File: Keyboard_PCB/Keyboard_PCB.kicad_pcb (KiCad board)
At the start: 4 copper layers, 305 x 132 mm, 1 part

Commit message: Keypad schematic progress
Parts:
- removed REF**: EC11E-Switch_No_MP, Custom:EC11E-Switch_No_MP
- added C14: 10u, Capacitor_SMD:C_0603_1608Metric, F.Cu at (181.6, 152.0)
- added C15: 56p, Capacitor_SMD:C_0603_1608Metric, F.Cu at (181.6, 154.5)
- added C16: 22u, Capacitor_SMD:C_0603_1608Metric, F.Cu at (181.6, 157.1)
- added C17: 22u, Capacitor_SMD:C_0603_1608Metric, F.Cu at (181.6, 159.6)
- added C18: 100n, Capacitor_SMD:C_0603_1608Metric, F.Cu at (242.3, 128.0)
- added C19: 12p, Capacitor_SMD:C_0603_1608Metric, F.Cu at (242.3, 130.5)
- added C20: 12p, Capacitor_SMD:C_0603_1608Metric, F.Cu at (242.3, 133.0)
- added C21: 12p, Capacitor_SMD:C_0603_1608Metric, F.Cu at (242.3, 135.5)
- added C22: 12p, Capacitor_SMD:C_0603_1608Metric, F.Cu at (242.3, 138.0)
- added D1: D_Small, Diode_SMD:D_SOD-323, F.Cu at (112.6, 101.9)
- added D10: D_Small, Diode_SMD:D_SOD-323, F.Cu at (121.2, 104.8)
- added D11: D_Small, Diode_SMD:D_SOD-323, F.Cu at (121.2, 107.8)
- added D12: D_Small, Diode_SMD:D_SOD-323, F.Cu at (121.2, 110.7)
- added D2: D_Small, Diode_SMD:D_SOD-323, F.Cu at (112.6, 104.8)
- added D3: D_Small, Diode_SMD:D_SOD-323, F.Cu at (112.6, 107.8)
- added D4: D_Small, Diode_SMD:D_SOD-323, F.Cu at (112.6, 110.7)
- added D5: D_Small, Diode_SMD:D_SOD-323, F.Cu at (116.9, 101.9)
- added D6: D_Small, Diode_SMD:D_SOD-323, F.Cu at (116.9, 104.8)
- added D7: D_Small, Diode_SMD:D_SOD-323, F.Cu at (116.9, 107.8)
- added D8: D_Small, Diode_SMD:D_SOD-323, F.Cu at (116.9, 110.7)
- added D9: D_Small, Diode_SMD:D_SOD-323, F.Cu at (121.2, 101.9)
- added J5: Conn_ARM_SWD_TagConnect_TC2030, Connector:Tag-Connect_TC2030-IDC-FP_2x03_P1.27mm_Vertical, F.Cu at (249.1, 131.5)
- added J6: CH_USB_C, Connector_USB:USB_C_Receptacle_HCTL_HC-TYPE-C-16P-01A, F.Cu at (211.9, 89.0)
- added L3: 1u, Inductor_SMD:L_APV_ANR4018, F.Cu at (186.5, 159.8)
- added R10: 10k, Resistor_SMD:R_0603_1608Metric, F.Cu at (242.3, 143.0)
- added R11: 320k, Resistor_SMD:R_0603_1608Metric, F.Cu at (181.6, 164.6)
- added R12: 5k1, Resistor_SMD:R_0603_1608Metric, F.Cu at (213.3, 94.9)
- added R8: 10k, Resistor_SMD:R_0603_1608Metric, F.Cu at (242.3, 140.5)
- added R9: 1M, Resistor_SMD:R_0603_1608Metric, F.Cu at (181.6, 162.1)
- added SW1: 0, Button_Switch_Keyboard:SW_Cherry_MX_1.00u_PCB, F.Cu at (134.5, 87.2)
- added SW10: 9, Button_Switch_Keyboard:SW_Cherry_MX_1.00u_PCB, F.Cu at (179.8, 87.2)
- added SW11: 10, Button_Switch_Keyboard:SW_Cherry_MX_1.00u_PCB, F.Cu at (179.8, 102.3)
- added SW12: 11, Button_Switch_Keyboard:SW_Cherry_MX_1.00u_PCB, F.Cu at (179.8, 117.4)
- added SW13: BOOT, Button_Switch_SMD:SW_SPST_PTS810, F.Cu at (247.7, 138.6)
- added SW14: NRST, Button_Switch_SMD:SW_SPST_PTS810, F.Cu at (247.7, 143.4)
- added SW2: 1, Button_Switch_Keyboard:SW_Cherry_MX_1.00u_PCB, F.Cu at (134.5, 102.3)
- added SW3: 2, Button_Switch_Keyboard:SW_Cherry_MX_1.00u_PCB, F.Cu at (134.5, 117.4)
- added SW4: 3, Button_Switch_Keyboard:SW_Cherry_MX_1.00u_PCB, F.Cu at (149.6, 87.2)
- added SW5: 4, Button_Switch_Keyboard:SW_Cherry_MX_1.00u_PCB, F.Cu at (149.6, 102.3)
- added SW6: 5, Button_Switch_Keyboard:SW_Cherry_MX_1.00u_PCB, F.Cu at (149.6, 117.4)
- added SW7: 6, Button_Switch_Keyboard:SW_Cherry_MX_1.00u_PCB, F.Cu at (164.7, 87.2)
- added SW8: 7, Button_Switch_Keyboard:SW_Cherry_MX_1.00u_PCB, F.Cu at (164.7, 102.3)
- added SW9: 8, Button_Switch_Keyboard:SW_Cherry_MX_1.00u_PCB, F.Cu at (164.7, 117.4)
- added TP1: 3V3, TestPoint:TestPoint_Pad_D1.5mm, F.Cu at (191.1, 158.8)
- added U1: STM32U385VGI6, Marijn:UFBGA-100_7x7mm, F.Cu at (149.0, 163.3)
- added U2: EMMC32G-TS0A-01002, Marijn:FBGA153_13X11.5X0.8, F.Cu at (134.8, 161.9)
- added U3: ISL91127IRAZ, Package_DFN_QFN:QFN-20-1EP_4x4mm_P0.5mm_EP2.7x2.7mm_ThermalVias, F.Cu at (186.8, 153.9)
- added U6: USBLC6-2SC6, Package_TO_SOT_SMD:SOT-23-6, F.Cu at (208.7, 96.1)
- added Y3: 25MHz, Crystal:Crystal_SMD_3225-4Pin_3.2x2.5mm, F.Cu at (253.7, 138.5)
- added Y4: 32.786KHz, Crystal:Crystal_SMD_3215-2Pin_3.2x1.5mm, F.Cu at (253.6, 142.5)
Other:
- board outline removed
- copper layers 4 -> 6

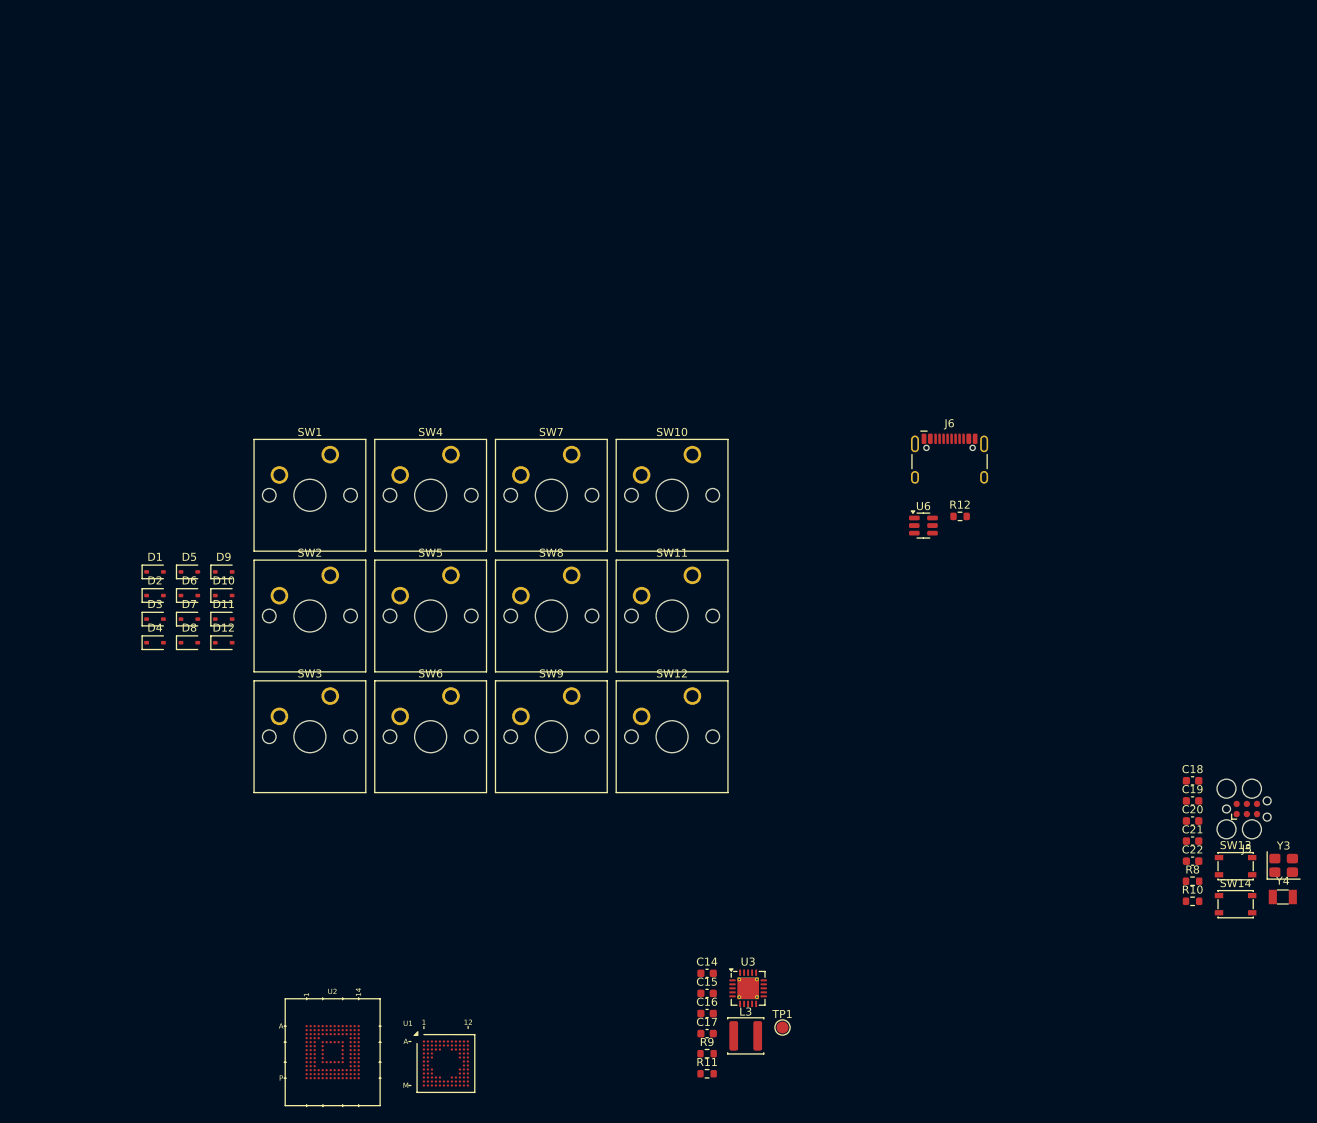
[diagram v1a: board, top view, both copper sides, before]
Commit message: STM32U385 pin assignment progress
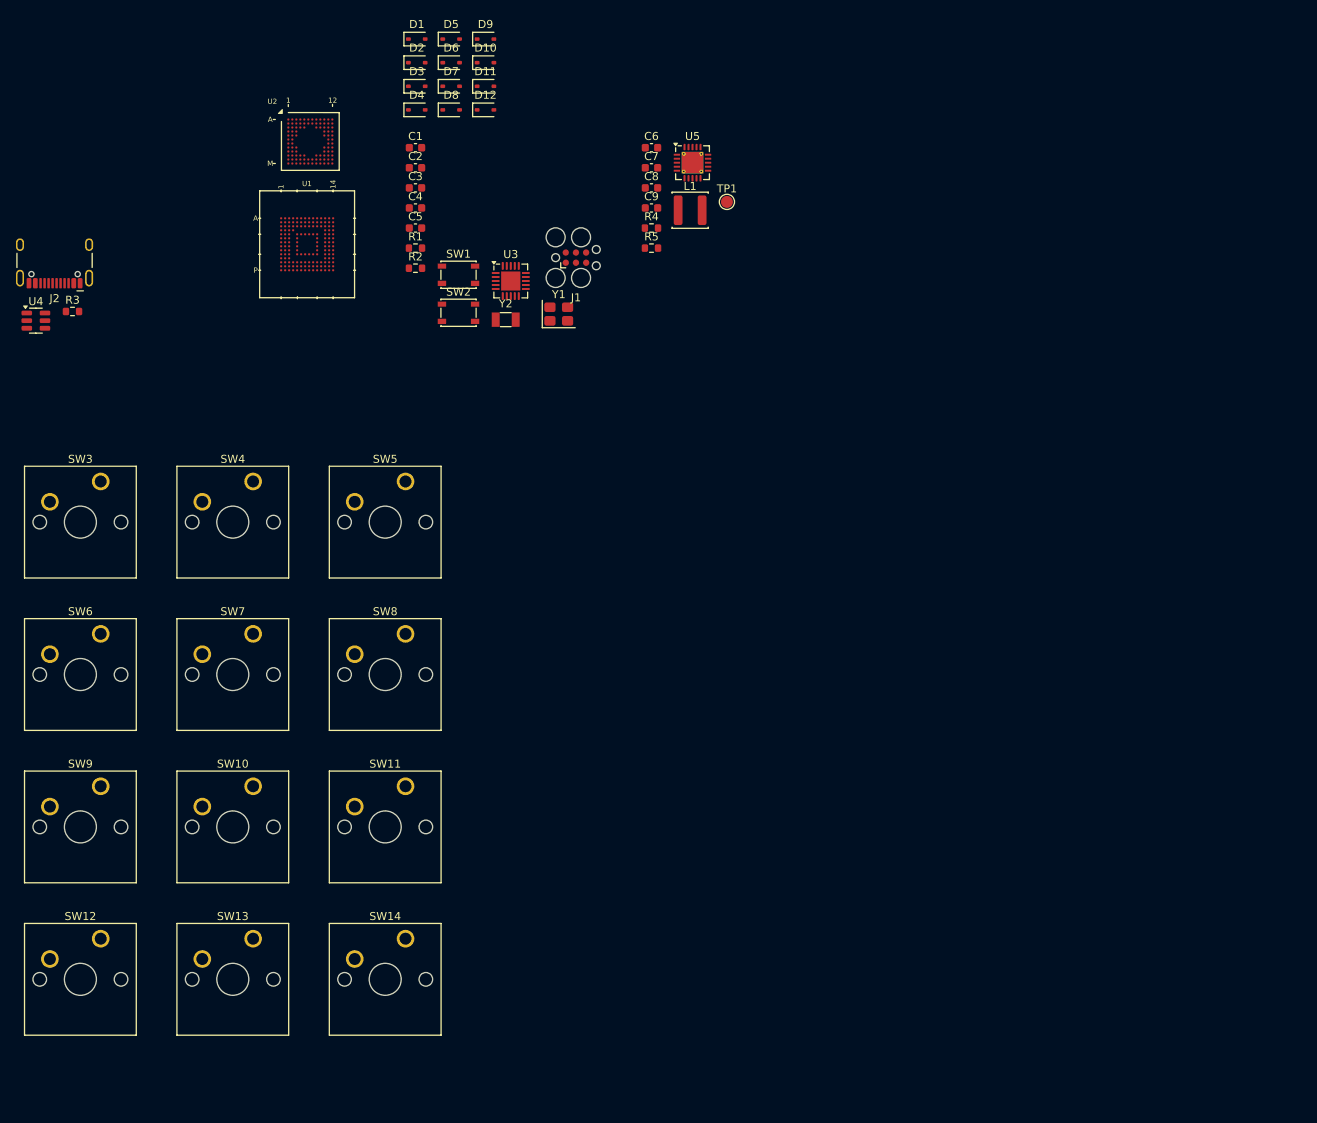
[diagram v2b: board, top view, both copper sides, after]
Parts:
- removed C14: 10u, Capacitor_SMD:C_0603_1608Metric
- removed C15: 56p, Capacitor_SMD:C_0603_1608Metric
- removed C16, C17: 22u, Capacitor_SMD:C_0603_1608Metric
- removed C18: 100n, Capacitor_SMD:C_0603_1608Metric
- removed C19, C20, C21, C22: 12p, Capacitor_SMD:C_0603_1608Metric
- removed J5: Conn_ARM_SWD_TagConnect_TC2030, Connector:Tag-Connect_TC2030-IDC-FP_2x03_P1.27mm_Vertical
- removed J6: CH_USB_C, Connector_USB:USB_C_Receptacle_HCTL_HC-TYPE-C-16P-01A
- removed L3: 1u, Inductor_SMD:L_APV_ANR4018
- removed R10, R8: 10k, Resistor_SMD:R_0603_1608Metric
- removed R11: 320k, Resistor_SMD:R_0603_1608Metric
- removed R12: 5k1, Resistor_SMD:R_0603_1608Metric
- removed R9: 1M, Resistor_SMD:R_0603_1608Metric
- removed U6: USBLC6-2SC6, Package_TO_SOT_SMD:SOT-23-6
- removed Y3: 25MHz, Crystal:Crystal_SMD_3225-4Pin_3.2x2.5mm
- removed Y4: 32.786KHz, Crystal:Crystal_SMD_3215-2Pin_3.2x1.5mm
- added C1: 100n, Capacitor_SMD:C_0603_1608Metric, F.Cu at (145.2, 48.8)
- added C2: 12p, Capacitor_SMD:C_0603_1608Metric, F.Cu at (145.2, 51.3)
- added C3: 12p, Capacitor_SMD:C_0603_1608Metric, F.Cu at (145.2, 53.8)
- added C4: 12p, Capacitor_SMD:C_0603_1608Metric, F.Cu at (145.2, 56.4)
- added C5: 12p, Capacitor_SMD:C_0603_1608Metric, F.Cu at (145.2, 58.9)
- added C6: 10u, Capacitor_SMD:C_0603_1608Metric, F.Cu at (174.7, 48.8)
- added C7: 56p, Capacitor_SMD:C_0603_1608Metric, F.Cu at (174.7, 51.3)
- added C8: 22u, Capacitor_SMD:C_0603_1608Metric, F.Cu at (174.7, 53.8)
- added C9: 22u, Capacitor_SMD:C_0603_1608Metric, F.Cu at (174.7, 56.4)
- added J1: Conn_ARM_SWD_TagConnect_TC2030, Connector:Tag-Connect_TC2030-IDC-FP_2x03_P1.27mm_Vertical, F.Cu at (165.2, 62.6)
- added J2: CH_USB_C, Connector_USB:USB_C_Receptacle_HCTL_HC-TYPE-C-16P-01A, F.Cu at (100.1, 62.0)
- added L1: 1u, Inductor_SMD:L_APV_ANR4018, F.Cu at (179.5, 56.6)
- added R1: 10k, Resistor_SMD:R_0603_1608Metric, F.Cu at (145.2, 61.4)
- added R2: 10k, Resistor_SMD:R_0603_1608Metric, F.Cu at (145.2, 63.9)
- added R3: 5k1, Resistor_SMD:R_0603_1608Metric, F.Cu at (102.3, 69.3)
- added R4: 1M, Resistor_SMD:R_0603_1608Metric, F.Cu at (174.7, 58.9)
- added R5: 320k, Resistor_SMD:R_0603_1608Metric, F.Cu at (174.7, 61.4)
- added U4: USBLC6-2SC6, Package_TO_SOT_SMD:SOT-23-6, F.Cu at (97.7, 70.4)
- added U5: ISL91127IRAZ, Package_DFN_QFN:QFN-20-1EP_4x4mm_P0.5mm_EP2.7x2.7mm_ThermalVias, F.Cu at (179.8, 50.7)
- added Y1: 25MHz, Crystal:Crystal_SMD_3225-4Pin_3.2x2.5mm, F.Cu at (163.1, 69.6)
- added Y2: 32.786KHz, Crystal:Crystal_SMD_3215-2Pin_3.2x1.5mm, F.Cu at (156.5, 70.3)
- SW1: value 0 -> BOOT; footprint Button_Switch_Keyboard:SW_Cherry_MX_1.00u_PCB -> Button_Switch_SMD:SW_SPST_PTS810
- SW10: value 9 -> 7
- SW11: value 10 -> 8
- SW12: value 11 -> 9
- SW13: value BOOT -> 10; footprint Button_Switch_SMD:SW_SPST_PTS810 -> Button_Switch_Keyboard:SW_Cherry_MX_1.00u_PCB
- SW14: value NRST -> 11; footprint Button_Switch_SMD:SW_SPST_PTS810 -> Button_Switch_Keyboard:SW_Cherry_MX_1.00u_PCB
- SW2: value 1 -> NRST; footprint Button_Switch_Keyboard:SW_Cherry_MX_1.00u_PCB -> Button_Switch_SMD:SW_SPST_PTS810
- SW3: value 2 -> 0
- SW4: value 3 -> 1
- SW5: value 4 -> 2
- SW6: value 5 -> 3
- SW7: value 6 -> 4
- SW8: value 7 -> 5
- SW9: value 8 -> 6
- U1: value STM32U385VGI6 -> EMMC32G-TS0A-01002; footprint Marijn:UFBGA-100_7x7mm -> Marijn:FBGA153_13X11.5X0.8
- U2: value EMMC32G-TS0A-01002 -> STM32U385VGI6; footprint Marijn:FBGA153_13X11.5X0.8 -> Marijn:UFBGA-100_7x7mm
- U3: value ISL91127IRAZ -> CC2500; footprint Package_DFN_QFN:QFN-20-1EP_4x4mm_P0.5mm_EP2.7x2.7mm_ThermalVias -> Package_DFN_QFN:Texas_RGP0020H_VQFN-20-1EP_4x4mm_P0.5mm_EP2.4x2.4mm
- moved SW13 123.1 mm to (124.9, 147.7)
- moved U2 113.9 mm to (132.0, 48.0)
- moved U1 103.9 mm to (131.6, 60.9)
- moved SW14 103.9 mm to (143.9, 147.7)
- moved TP1 103.4 mm to (184.1, 55.6)
- moved U3 93.3 mm to (157.1, 65.5)
- moved SW12 79.9 mm to (105.8, 147.7)
- moved D1 74.2 mm to (145.4, 35.2)
- moved D12 74.2 mm to (153.9, 44.1)
- moved D4 74.2 mm to (145.4, 44.1)
- moved D5 74.2 mm to (149.6, 35.2)
- moved D8 74.2 mm to (149.6, 44.1)
- moved D9 74.2 mm to (153.9, 35.2)
- moved D6 74.2 mm to (149.6, 38.2)
- moved D7 74.2 mm to (149.6, 41.1)
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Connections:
- D1 pad 1: /KEY_GRID/ROW_0 -> /ROW_0
- D10 pad 1: /KEY_GRID/ROW_3 -> /ROW_3
- D11 pad 1: /KEY_GRID/ROW_3 -> /ROW_3
- D12 pad 1: /KEY_GRID/ROW_3 -> /ROW_3
- D2 pad 1: /KEY_GRID/ROW_0 -> /ROW_0
- D3 pad 1: /KEY_GRID/ROW_0 -> /ROW_0
- D4 pad 1: /KEY_GRID/ROW_1 -> /ROW_1
- D5 pad 1: /KEY_GRID/ROW_1 -> /ROW_1
- D6 pad 1: /KEY_GRID/ROW_1 -> /ROW_1
- D7 pad 1: /KEY_GRID/ROW_2 -> /ROW_2
- D8 pad 1: /KEY_GRID/ROW_2 -> /ROW_2
- D9 pad 1: /KEY_GRID/ROW_2 -> /ROW_2
- SW1 pad 1: /KEY_GRID/COL_0 -> +3V3
- SW1 pad 2: Net-(D1-A) -> /BOOT
- SW10 pad 1: /KEY_GRID/COL_0 -> /COL_1
- SW10 pad 2: Net-(D10-A) -> Net-(D8-A)
- SW11 pad 1: /KEY_GRID/COL_1 -> /COL_2
- SW11 pad 2: Net-(D11-A) -> Net-(D9-A)
- SW12 pad 1: /KEY_GRID/COL_2 -> /COL_0
- SW12 pad 2: Net-(D12-A) -> Net-(D10-A)
- SW13 pad 1: +3V3 -> /COL_1
- SW13 pad 2: /BOOT -> Net-(D11-A)
- SW14 pad 1: /NRST -> /COL_2
- SW14 pad 2: GND -> Net-(D12-A)
- SW2 pad 1: /KEY_GRID/COL_1 -> /NRST
- SW2 pad 2: Net-(D2-A) -> GND
- SW3 pad 1: /KEY_GRID/COL_2 -> /COL_0
- SW3 pad 2: Net-(D3-A) -> Net-(D1-A)
- SW4 pad 1: /KEY_GRID/COL_0 -> /COL_1
- SW4 pad 2: Net-(D4-A) -> Net-(D2-A)
- SW5 pad 1: /KEY_GRID/COL_1 -> /COL_2
- SW5 pad 2: Net-(D5-A) -> Net-(D3-A)
- SW6 pad 1: /KEY_GRID/COL_2 -> /COL_0
- SW6 pad 2: Net-(D6-A) -> Net-(D4-A)
- SW7 pad 1: /KEY_GRID/COL_0 -> /COL_1
- SW7 pad 2: Net-(D7-A) -> Net-(D5-A)
- SW8 pad 1: /KEY_GRID/COL_1 -> /COL_2
- SW8 pad 2: Net-(D8-A) -> Net-(D6-A)
- SW9 pad 1: /KEY_GRID/COL_2 -> /COL_0
- SW9 pad 2: Net-(D9-A) -> Net-(D7-A)
- U1 pad A1: unconnected-(U1-PE3-PadA1) -> (no net)
- U1 pad A10: unconnected-(U1-PA14-PadA10) -> (no net)
- U1 pad A11: unconnected-(U1-PA13-PadA11) -> (no net)
- U1 pad A12: unconnected-(U1-PA12-PadA12) -> (no net)
- U1 pad A2: unconnected-(U1-PE1-PadA2) -> (no net)
- U1 pad A3: unconnected-(U1-PB8-PadA3) -> /eMMC_D0
- U1 pad A4: unconnected-(U1-PH3-BOOT0-PadA4) -> /eMMC_D1
- U1 pad A5: unconnected-(U1-PD7-PadA5) -> /eMMC_D2
- U1 pad A6: unconnected-(U1-PD5-PadA6) -> GND
- U1 pad A8: unconnected-(U1-PB3-PadA8) -> (no net)
- U1 pad A9: unconnected-(U1-PA15-PadA9) -> (no net)
- U1 pad B1: unconnected-(U1-PE4-PadB1) -> (no net)
- U1 pad B10: unconnected-(U1-PC12-PadB10) -> (no net)
- U1 pad B11: unconnected-(U1-PC10-PadB11) -> (no net)
- U1 pad B12: unconnected-(U1-PA11-PadB12) -> (no net)
- U1 pad B2: unconnected-(U1-PE2-PadB2) -> /eMMC_D3
- U1 pad B3: unconnected-(U1-PB9-PadB3) -> /eMMC_D4
- U1 pad B4: unconnected-(U1-PB7-PadB4) -> /eMMC_D5
- U1 pad B5: unconnected-(U1-PB6-PadB5) -> /eMMC_D6
- U1 pad B6: unconnected-(U1-PD6-PadB6) -> /eMMC_D7
- U1 pad B7: unconnected-(U1-PD4-PadB7) -> (no net)
- U1 pad B8: unconnected-(U1-PD3-PadB8) -> (no net)
- U1 pad B9: unconnected-(U1-PD1-PadB9) -> (no net)
- U1 pad C1: unconnected-(U1-PC13-PadC1) -> (no net)
- U1 pad C10: unconnected-(U1-PC11-PadC10) -> (no net)
- U1 pad C11: unconnected-(U1-VDDUSB-PadC11) -> (no net)
- U1 pad C12: unconnected-(U1-PA10-PadC12) -> (no net)
- U1 pad C3: unconnected-(U1-PE0-PadC3) -> (no net)
- U1 pad C4: unconnected-(U1-VDD-PadC4) -> GND
- U1 pad C5: unconnected-(U1-PB5-PadC5) -> (no net)
- U1 pad C8: unconnected-(U1-PD2-PadC8) -> (no net)
- U1 pad C9: unconnected-(U1-PD0-PadC9) -> (no net)
- U1 pad D1: unconnected-(U1-PC14-OSC32_IN-PadD1) -> (no net)
- U1 pad D12: unconnected-(U1-PC9-PadD12) -> (no net)
- U1 pad D2: unconnected-(U1-PE6-PadD2) -> (no net)
- U1 pad D3: unconnected-(U1-VSS-PadD3) -> (no net)
- U1 pad E1: unconnected-(U1-PC15-OSC32_OUT-PadE1) -> (no net)
- U1 pad E12: unconnected-(U1-PC6-PadE12) -> (no net)
- U1 pad E2: unconnected-(U1-VBAT-PadE2) -> (no net)
- U1 pad E3: unconnected-(U1-VSS-PadE3) -> (no net)
- U1 pad F1: unconnected-(U1-PH0-OSC_IN-PadF1) -> (no net)
- U1 pad F12: unconnected-(U1-VSS-PadF12) -> (no net)
- U1 pad F2: unconnected-(U1-VSS-PadF2) -> (no net)
- U1 pad G1: unconnected-(U1-PH1-OSC_OUT-PadG1) -> (no net)
- U1 pad G12: unconnected-(U1-VDD-PadG12) -> (no net)
- U1 pad G2: unconnected-(U1-VDD-PadG2) -> (no net)
- U1 pad H1: unconnected-(U1-PC0-PadH1) -> (no net)
- U1 pad H10: unconnected-(U1-PD15-PadH10) -> GND
- U1 pad H12: unconnected-(U1-PD13-PadH12) -> (no net)
- U1 pad H2: unconnected-(U1-NRST-PadH2) -> (no net)
- U1 pad H3: unconnected-(U1-VDD-PadH3) -> (no net)
- U1 pad J1: unconnected-(U1-VSSA-PadJ1) -> (no net)
- U1 pad J10: unconnected-(U1-PD12-PadJ10) -> VCC
- U1 pad J12: unconnected-(U1-PD10-PadJ12) -> (no net)
- U1 pad J2: unconnected-(U1-PC1-PadJ2) -> (no net)
- U1 pad J3: unconnected-(U1-PC2-PadJ3) -> (no net)
- U1 pad K1: unconnected-(U1-VREF--PadK1) -> (no net)
- U1 pad K12: unconnected-(U1-PB13-PadK12) -> (no net)
- U1 pad K2: unconnected-(U1-PC3-PadK2) -> (no net)
- U1 pad K3: unconnected-(U1-PA2-PadK3) -> (no net)
- U1 pad K5: unconnected-(U1-PC4-PadK5) -> /eMMC_NRST
- U1 pad K8: unconnected-(U1-PD9-PadK8) -> GND
- U1 pad K9: unconnected-(U1-PD8-PadK9) -> VCC
- U1 pad L1: unconnected-(U1-VREF+-PadL1) -> (no net)
- U1 pad L12: unconnected-(U1-PB12-PadL12) -> (no net)
- U1 pad L2: unconnected-(U1-PA0-PadL2) -> (no net)
- U1 pad L3: unconnected-(U1-PA3-PadL3) -> (no net)
- U1 pad M1: unconnected-(U1-VDDA-PadM1) -> (no net)
- U1 pad M10: unconnected-(U1-PE13-PadM10) -> (no net)
- U1 pad M11: unconnected-(U1-PE14-PadM11) -> (no net)
- U1 pad M12: unconnected-(U1-PE15-PadM12) -> (no net)
- U1 pad M2: unconnected-(U1-PA1-PadM2) -> (no net)
- U1 pad M3: unconnected-(U1-PA4-PadM3) -> (no net)
- U1 pad M4: unconnected-(U1-PA7-PadM4) -> VCC_q
- U1 pad M5: unconnected-(U1-PB0-PadM5) -> /eMMC_CMD
- U1 pad M6: unconnected-(U1-PB1-PadM6) -> /eMMC_CLK
- U1 pad M7: unconnected-(U1-PE7-PadM7) -> (no net)
- U1 pad M8: unconnected-(U1-PE9-PadM8) -> (no net)
- U1 pad M9: unconnected-(U1-PE11-PadM9) -> (no net)
- U2 pad A1: (no net) -> /ROW_2
- U2 pad A10: (no net) -> /SWCLK
- U2 pad A11: (no net) -> /SWDIO
- U2 pad A12: (no net) -> /USB_DP
- U2 pad A2: (no net) -> /ROW_0
- U2 pad A3: unconnected-(U2-DAT0-PadA3) -> /eMMC_D4
- U2 pad A4: unconnected-(U2-DAT1-PadA4) -> /BOOT
- U2 pad A5: unconnected-(U2-DAT2-PadA5) -> /COL_2
- U2 pad A6: VSS -> /COL_0
- U2 pad A8: (no net) -> /SWO
- U2 pad A9: (no net) -> unconnected-(U2-PA15-PadA9)
- U2 pad B1: (no net) -> /ROW_3
- U2 pad B10: (no net) -> /eMMC_CLK
- U2 pad B11: (no net) -> /eMMC_D2
- U2 pad B12: (no net) -> /USB_DN
- U2 pad B2: unconnected-(U2-DAT3-PadB2) -> /ROW_1
- U2 pad B3: unconnected-(U2-DAT4-PadB3) -> /eMMC_D5
- U2 pad B6: unconnected-(U2-DAT7-PadB6) -> /COL_1
- U2 pad B7: (no net) -> unconnected-(U2-PD4-PadB7)
- U2 pad B8: (no net) -> unconnected-(U2-PD3-PadB8)
- U2 pad B9: (no net) -> unconnected-(U2-PD1-PadB9)
- U2 pad C1: (no net) -> unconnected-(U2-PC13-PadC1)
- U2 pad C10: (no net) -> /eMMC_D3
- U2 pad C11: (no net) -> unconnected-(U2-VDDUSB-PadC11)
- U2 pad C12: (no net) -> /eMMC_NRST
- U2 pad C3: (no net) -> unconnected-(U2-PE0-PadC3)
- U2 pad C4: VSS_q -> unconnected-(U2-VDD-PadC4)
- U2 pad C5: (no net) -> unconnected-(U2-PB5-PadC5)
- U2 pad C8: (no net) -> /eMMC_CMD
- U2 pad C9: (no net) -> unconnected-(U2-PD0-PadC9)
- U2 pad D1: (no net) -> /LSE_I
- U2 pad D12: (no net) -> /eMMC_D1
- U2 pad D2: (no net) -> unconnected-(U2-PE6-PadD2)
- U2 pad D3: (no net) -> unconnected-(U2-VSS-PadD3)
- U2 pad E1: (no net) -> /LSE_O
- U2 pad E10: unconnected-(U2-VSF-PadE10) -> /eMMC_D0
- U2 pad E12: (no net) -> /eMMC_D6
- U2 pad E2: (no net) -> unconnected-(U2-VBAT-PadE2)
- U2 pad E3: (no net) -> unconnected-(U2-VSS-PadE3)
- U2 pad F1: (no net) -> /HSE_I
- U2 pad F12: (no net) -> unconnected-(U2-VSS-PadF12)
- U2 pad F2: (no net) -> unconnected-(U2-VSS-PadF2)
- U2 pad G1: (no net) -> /HSE_O
- U2 pad G12: (no net) -> unconnected-(U2-VDD-PadG12)
- U2 pad G2: (no net) -> unconnected-(U2-VDD-PadG2)
- U2 pad H1: (no net) -> unconnected-(U2-PC0-PadH1)
- U2 pad H10: VSS -> unconnected-(U2-PD15-PadH10)
- U2 pad H12: (no net) -> unconnected-(U2-PD13-PadH12)
- U2 pad H2: (no net) -> /NRST
- U2 pad H3: (no net) -> unconnected-(U2-VDD-PadH3)
- U2 pad J1: (no net) -> unconnected-(U2-VSSA-PadJ1)
- U2 pad J10: VCC -> unconnected-(U2-PD12-PadJ10)
- U2 pad J12: (no net) -> unconnected-(U2-PD10-PadJ12)
- U2 pad J2: (no net) -> unconnected-(U2-PC1-PadJ2)
- U2 pad J3: (no net) -> unconnected-(U2-PC2-PadJ3)
- U2 pad K1: (no net) -> unconnected-(U2-VREF--PadK1)
- U2 pad K10: unconnected-(U2-VSF-PadK10) -> /OLED_SPI_MOSI
- U2 pad K12: (no net) -> /OLED_SPI_SCK
- U2 pad K2: (no net) -> unconnected-(U2-PC3-PadK2)
- U2 pad K3: (no net) -> unconnected-(U2-PA2-PadK3)
- U2 pad K8: VSS -> unconnected-(U2-PD9-PadK8)
- U2 pad K9: VCC -> unconnected-(U2-PD8-PadK9)
- U2 pad L1: (no net) -> unconnected-(U2-VREF+-PadL1)
- U2 pad L12: (no net) -> unconnected-(U2-PB12-PadL12)
- U2 pad L2: (no net) -> unconnected-(U2-PA0-PadL2)
- U2 pad L3: (no net) -> unconnected-(U2-PA3-PadL3)
- U2 pad M1: (no net) -> unconnected-(U2-VDDA-PadM1)
- U2 pad M10: (no net) -> unconnected-(U2-PE13-PadM10)
- U2 pad M11: (no net) -> /RF_SPI_MISO
- U2 pad M12: (no net) -> unconnected-(U2-PE15-PadM12)
- U2 pad M2: (no net) -> /RF_SPI_SCK
- U2 pad M3: (no net) -> /RF_SPI_NSS
- U2 pad M4: VCC_q -> /RF_SPI_MOSI
- U2 pad M7: (no net) -> unconnected-(U2-PE7-PadM7)
- U2 pad M8: (no net) -> unconnected-(U2-PE9-PadM8)
- U2 pad M9: (no net) -> unconnected-(U2-PE11-PadM9)
- U3 pad 1: Net-(L3-Pad2) -> /SPI_SCK
- U3 pad 10: +5V -> unconnected-(U3-XOSC_Q2-Pad10)
- U3 pad 11: +5V -> Net-(U3-AVDD-Pad11)
- U3 pad 12: +5V -> unconnected-(U3-RF_P-Pad12)
- U3 pad 13: GND -> unconnected-(U3-RF_N-Pad13)
- U3 pad 14: GND -> Net-(U3-AVDD-Pad11)
- U3 pad 15: Net-(U3-FB) -> Net-(U3-AVDD-Pad11)
- U3 pad 16: (no net) -> GND
- U3 pad 17: +3V3 -> unconnected-(U3-RBIAS-Pad17)
- U3 pad 18: +3V3 -> unconnected-(U3-VDD_GUARD-Pad18)
- U3 pad 19: +3V3 -> GND
- U3 pad 2: Net-(L3-Pad2) -> /SPI_MISO
- U3 pad 20: +3V3 -> /SPI_MOSI
- U3 pad 3: GND -> unconnected-(U3-GDO2-Pad3)
- U3 pad 4: Net-(L3-Pad1) -> unconnected-(U3-DVDD-Pad4)
- U3 pad 5: Net-(L3-Pad1) -> unconnected-(U3-DCOUPL-Pad5)
- U3 pad 6: +5V -> unconnected-(U3-GDO0(ATEST)-Pad6)
- U3 pad 7: +5V -> /SPI_NSS
- U3 pad 8: +5V -> unconnected-(U3-XOSC_Q1-Pad8)
- U3 pad 9: +5V -> Net-(U3-AVDD-Pad11)
